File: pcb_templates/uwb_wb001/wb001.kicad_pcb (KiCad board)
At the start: 2 copper layers, 40.1 x 22.2 mm, 1 part, among them J101 Conn_01x01

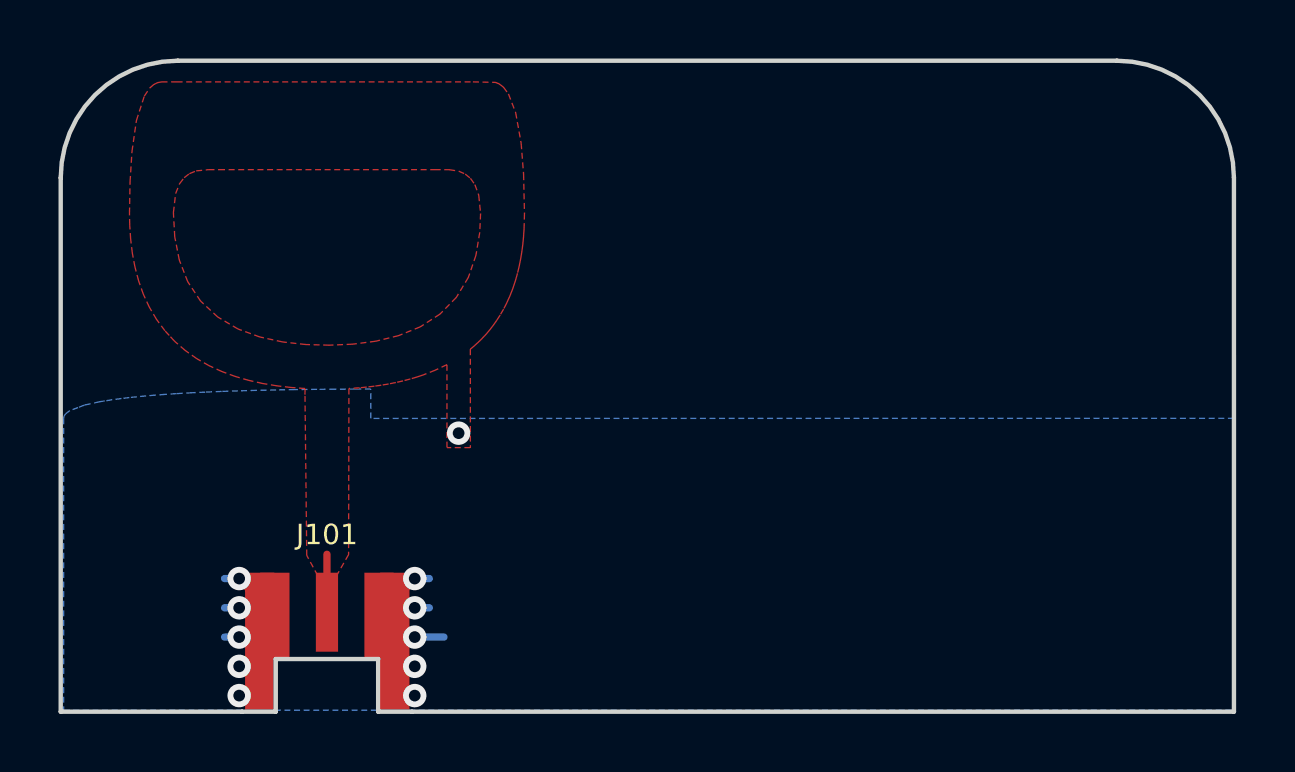
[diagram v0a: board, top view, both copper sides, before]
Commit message: Updated wb001 antenna
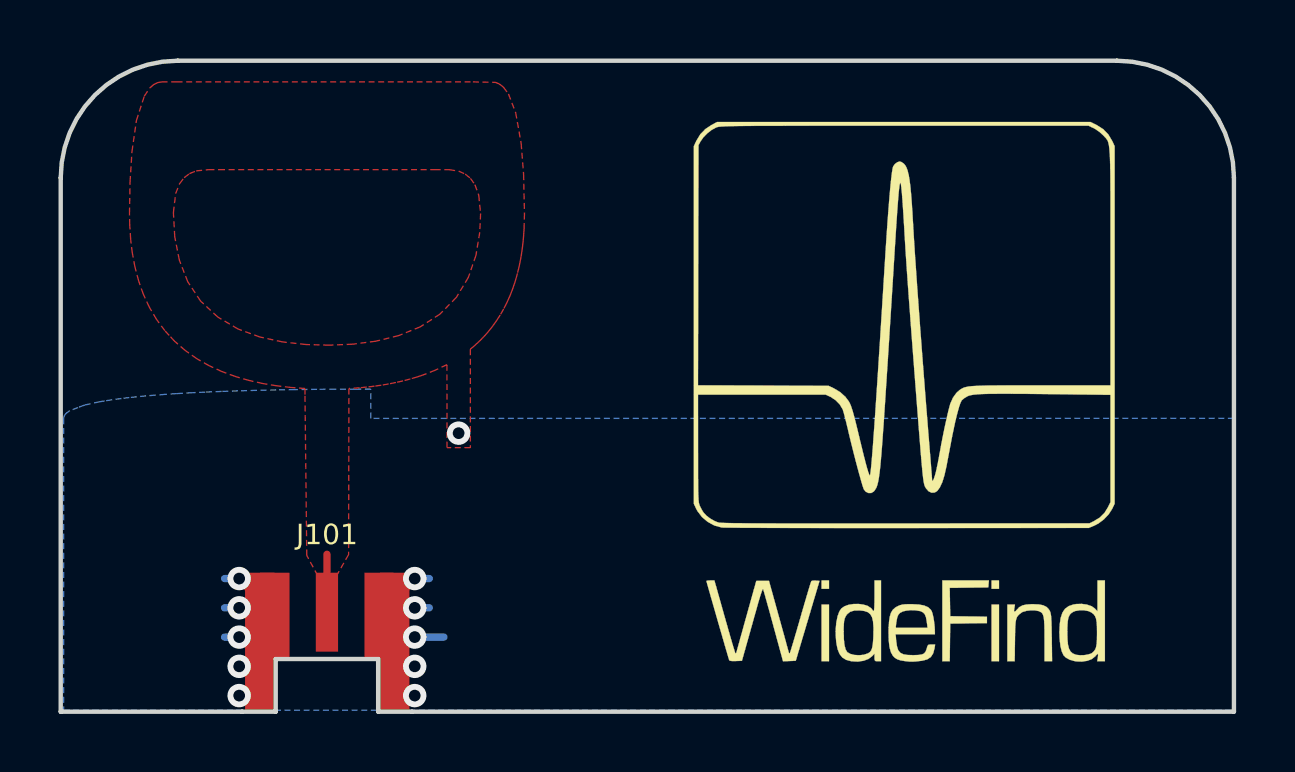
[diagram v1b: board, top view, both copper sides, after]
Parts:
- added G***: LOGO, logo:widefind_14.6x18.7, F.Cu at (177.2, 61.6)
